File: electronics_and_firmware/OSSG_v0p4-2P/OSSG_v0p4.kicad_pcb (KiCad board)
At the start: 4 copper layers, 85 x 9 mm, 73 parts, among them J1 Conn_01x05_Male, J2 Ext RGB, J3 USB_B_Micro, J4 Touch, J5 Ext. HUD (experimental), Q1 2SC4617R BR, Q2 2SC4617R BR, Q3 PMZ290UNE2YL, Q4 YJQD30P02A, SW1 SW_SPST, SW2 Power, U1 MP23DB01HPTR, U2 ESP32-PICO-D4, U3 CH9102F, U4 XC61CC3002MR, U5 AP5054HTC, U6 MAX17048, U7 NCP167BMX330TBG, U8 SY7088

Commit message: final V0.4 PCB as first manufacture run
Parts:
- moved R18 0.76 mm to (121.4, 78.6)
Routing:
- net Net-(R18-Pad2): track 1.23 -> 6.25 mm
- net +3V3: track 37.2 -> 34.6 mm
- net BATT1-: track 151.4 -> 152.4 mm
- net +5V: track 80.0 -> 81.0 mm
- net BATT+: track 79.8 -> 79.1 mm
- net Net-(Q3-Pad1): track 36.3 -> 36.9 mm

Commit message: updating schematic and PCB with minor changes
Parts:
- moved SW1 0.40 mm to (79.9, 76.5)
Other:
- board text added: "Open Source Smart Glasses V0.4a"
- board text removed: "Open Source Smart Glasses V0.4"

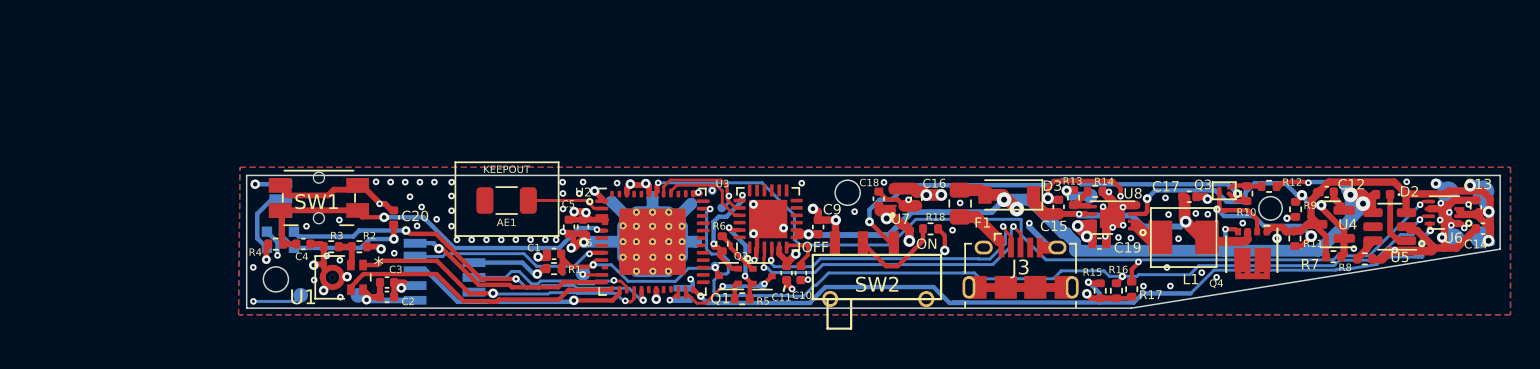
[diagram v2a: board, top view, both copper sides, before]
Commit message: add PSRAM, move button to bottom (thumb press)
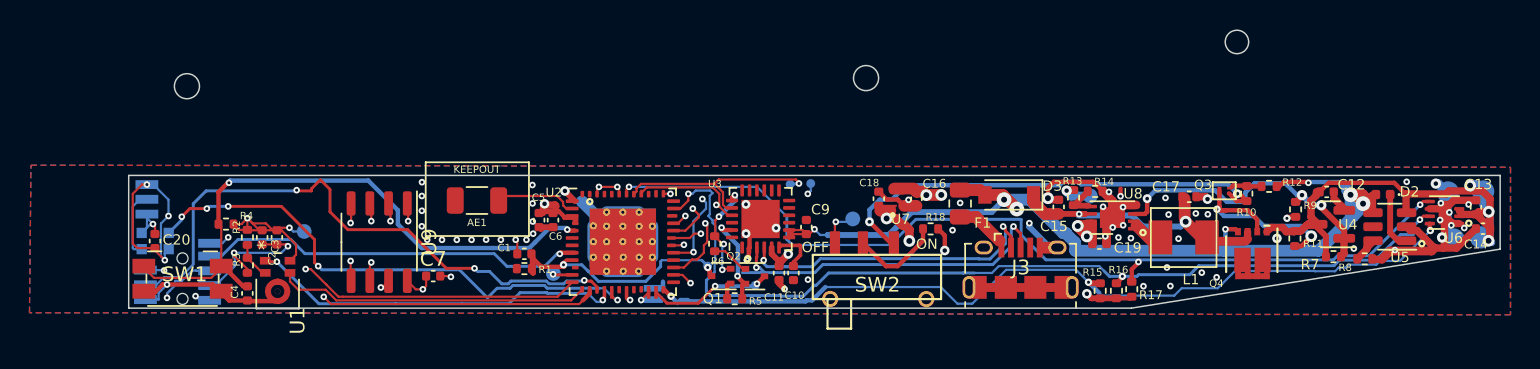
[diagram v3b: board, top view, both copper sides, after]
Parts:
- added C7: 100nF, Capacitor_SMD:C_0402_1005Metric, F.Cu at (87.7, 81.8)
- added U9: LY68L6400SLIT_PSRAM, Package_SO:SOP-8_3.9x4.9mm_P1.27mm, F.Cu at (84.0, 79.5)
- R15, R16: value 10K -> 4.7K
- moved TP9 37.8 mm to (116.1, 78.0)
- moved J5 22.3 mm to (68.2, 82.0)
- moved C20 16.3 mm to (68.8, 79.5)
- moved J1 13.9 mm to (72.5, 82.0)
- moved SW1 10.7 mm to (70.7, 82.0), turned to 0 degrees
- moved J2 9.10 mm to (68.3, 76.2), turned to 90 degrees
- moved C3 9.01 mm to (76.0, 79.2), turned to 90 degrees
- moved D1 8.49 mm to (68.8, 79.5)
- moved C2 8.49 mm to (77.0, 79.2), turned to -90 degrees
- moved R2 7.62 mm to (75.0, 79.2), turned to 90 degrees
- moved TP14 6.69 mm to (113.2, 75.5)
- moved R3 5.82 mm to (75.0, 81.1), turned to 90 degrees
- moved TP8 5.67 mm to (78.9, 78.8)
- moved C4 5.06 mm to (75.0, 83.0), turned to -90 degrees
- moved TP13 4.90 mm to (111.8, 75.6)
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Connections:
- U2 pad 26: unconnected-(U2-Pad26) -> VDD_SDIO
- U2 pad 27: unconnected-(U2-Pad27) -> SIO1
- U2 pad 29: unconnected-(U2-Pad29) -> PSRAM_CS
- U2 pad 30: unconnected-(U2-Pad30) -> SIO3
- U2 pad 31: unconnected-(U2-Pad31) -> SCLK
- U2 pad 32: unconnected-(U2-Pad32) -> SIO2
- U2 pad 33: unconnected-(U2-Pad33) -> SIO0
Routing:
- net SIO1: track 0.00 -> 33.1 mm, vias 0 -> 2
- net PSRAM_CS: track 0.00 -> 31.6 mm, vias 0 -> 3
- net SCLK: track 0.00 -> 30.0 mm, vias 0 -> 2
- net SIO2: track 0.00 -> 29.9 mm, vias 0 -> 2
- net BATT1-: track 152.7 -> 122.9 mm, vias 97 -> 66
- net SIO3: track 0.00 -> 29.1 mm, vias 0 -> 2
- net DAC: track 11.5 -> 40.5 mm, vias 1 -> 3
- net SIO0: track 0.00 -> 28.5 mm, vias 0 -> 2
- net VDD_SDIO: track 0.00 -> 23.2 mm, vias 0 -> 2
- net +5V: track 81.0 -> 100.9 mm, vias 6 -> 8
- net i2S2_CLK: track 14.9 -> 34.3 mm, vias 1 -> 2
- net SWITCH: track 26.7 -> 41.0 mm
- net i2S2_Data: track 13.4 -> 26.4 mm
- net i2S2_WS: track 13.9 -> 26.8 mm, vias 1 -> 2
- net RGB: track 26.7 -> 36.4 mm, vias 3 -> 5
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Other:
- board size 85 x 9 mm -> 93 x 18.8 mm
